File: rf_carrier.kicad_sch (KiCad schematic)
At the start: 1 part

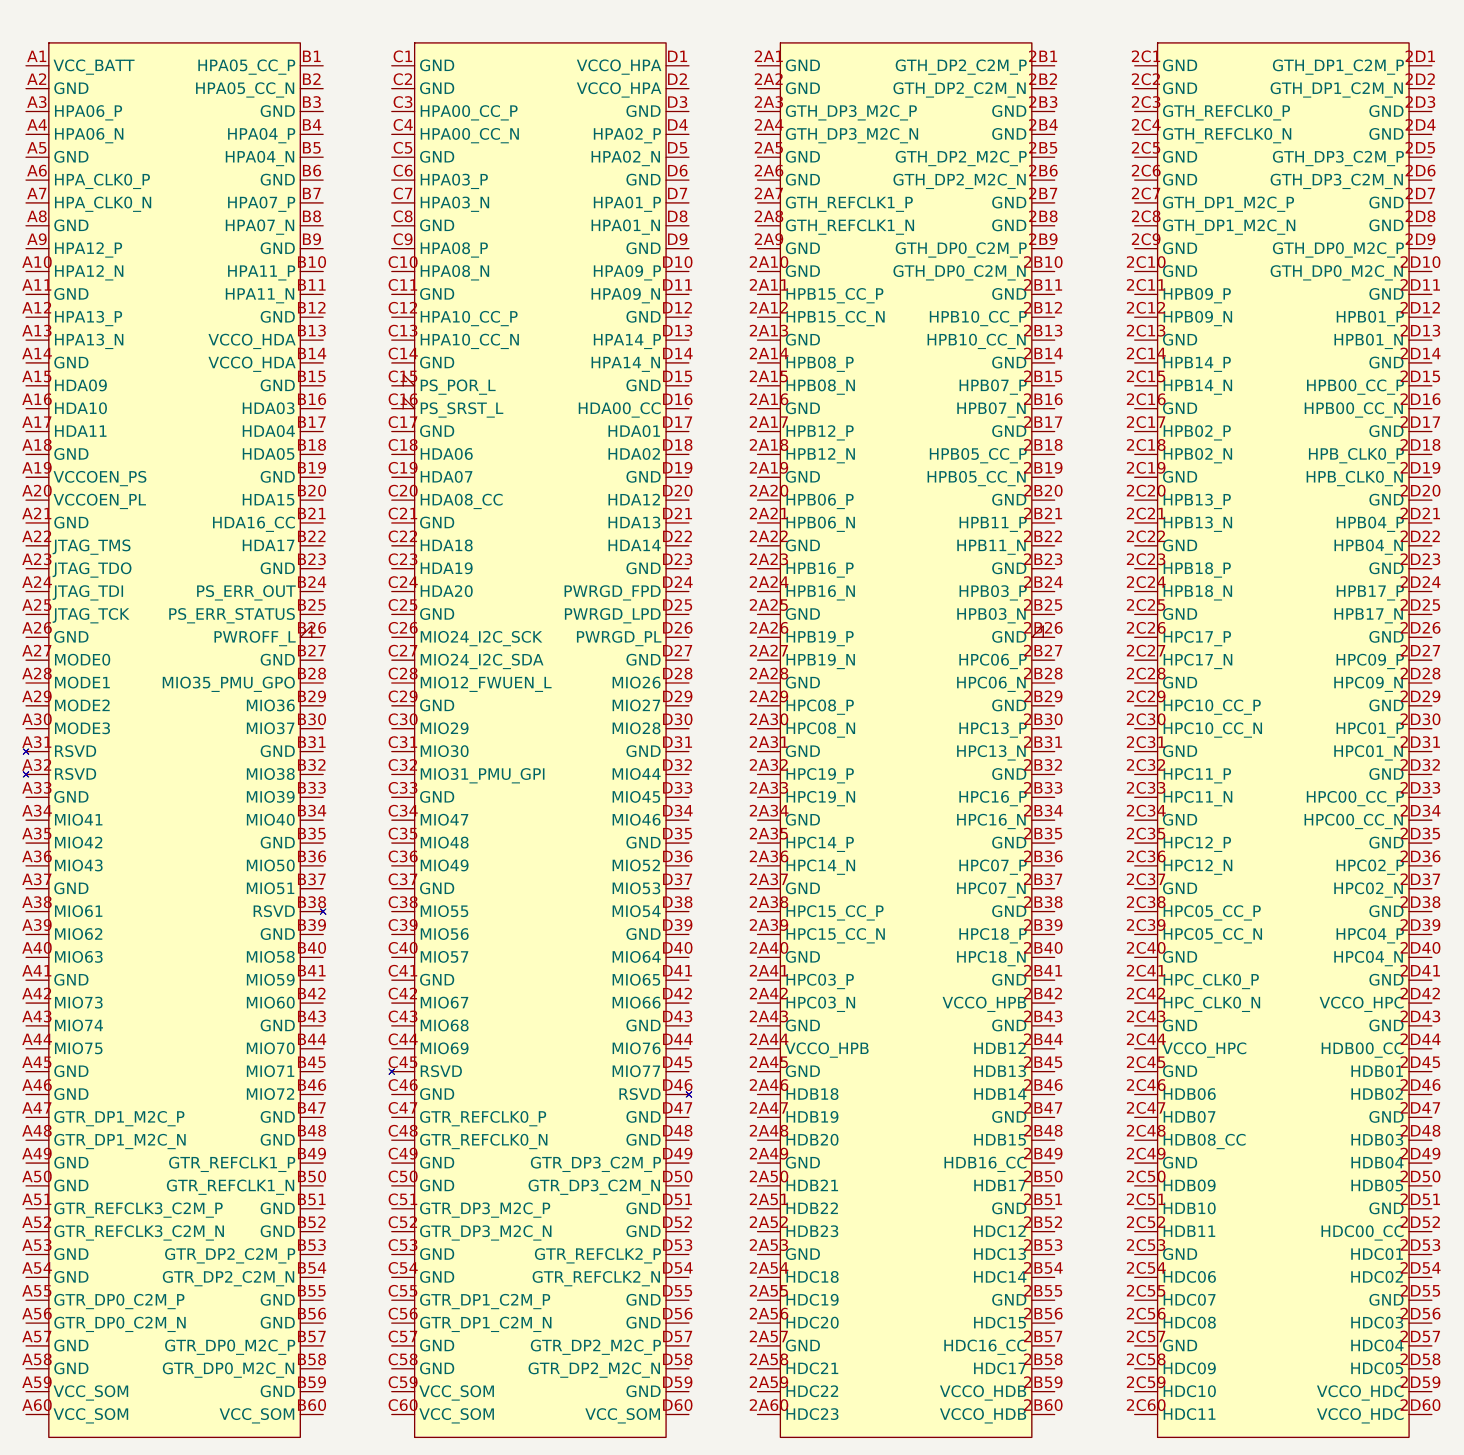
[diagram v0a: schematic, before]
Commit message: MIO pins hier labels and MIO25 symbol pin label fix
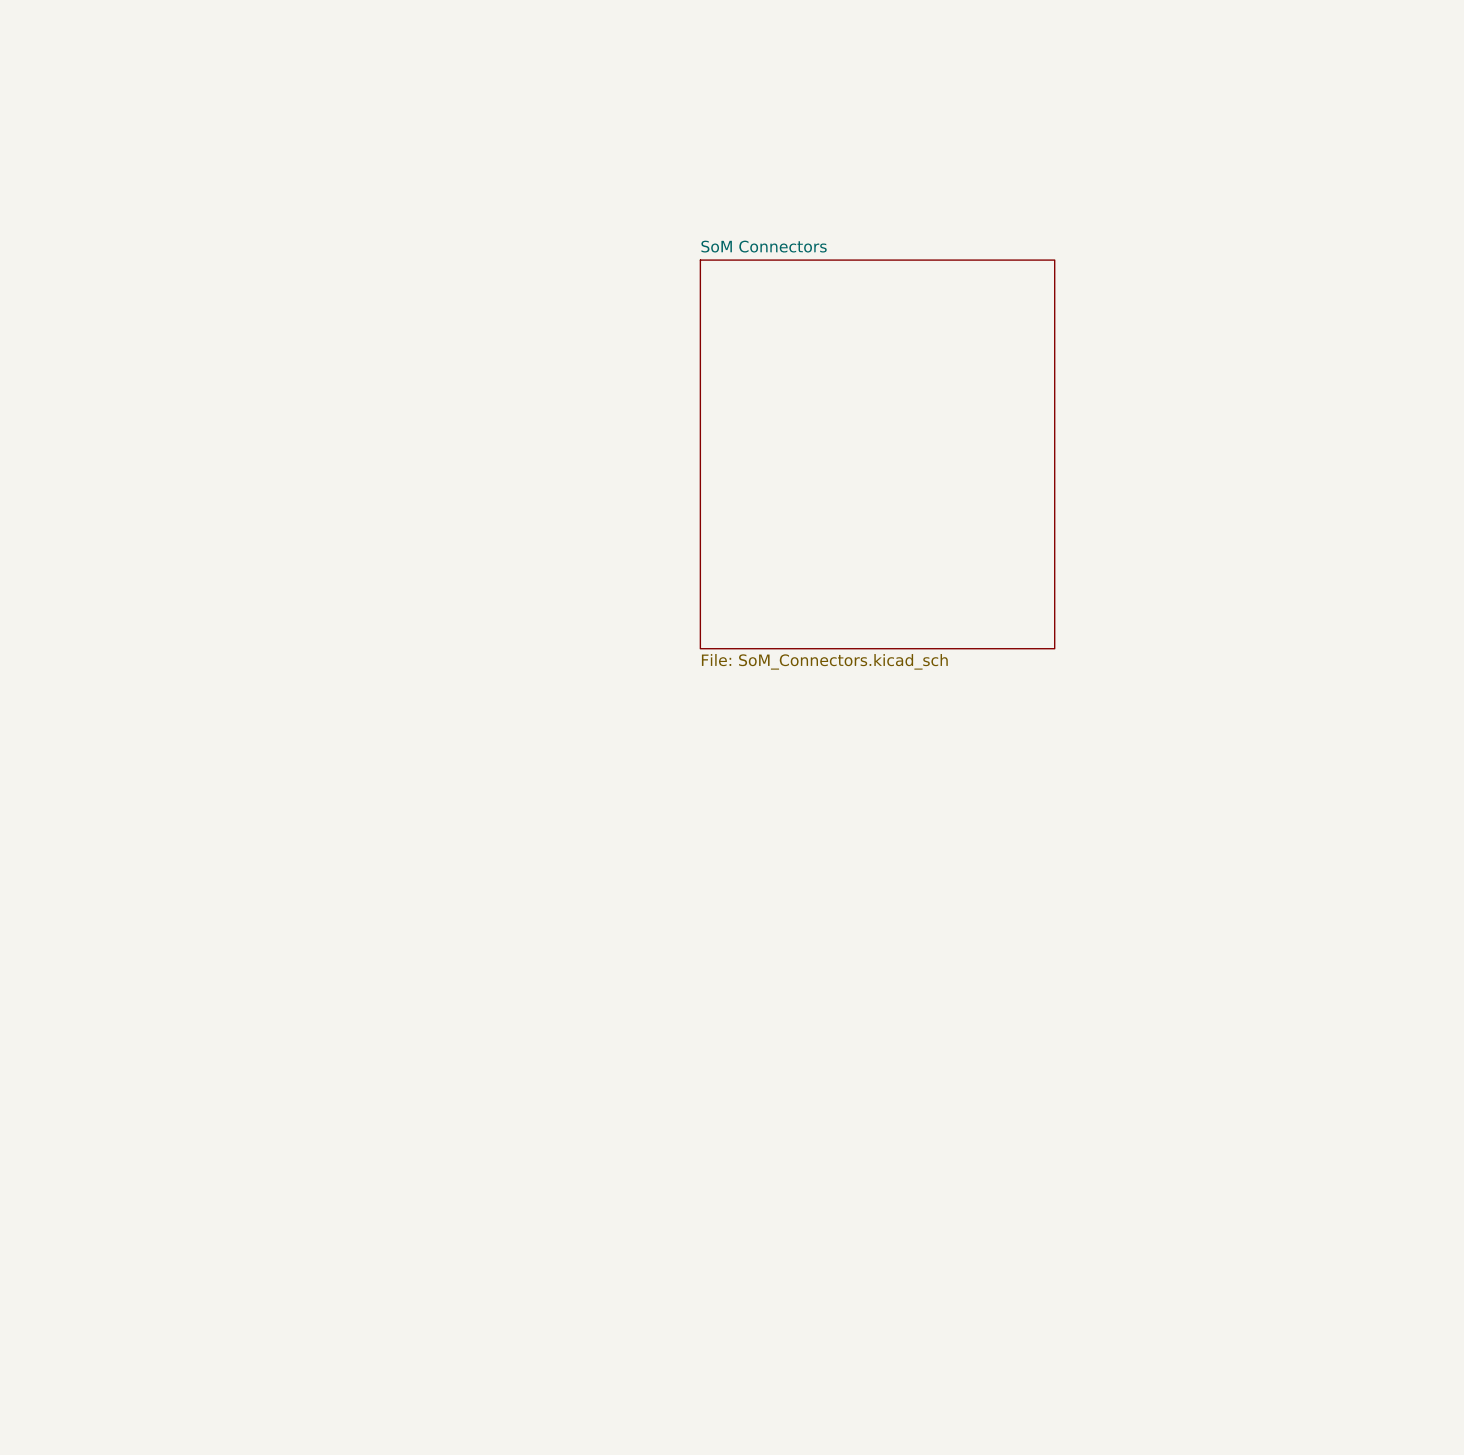
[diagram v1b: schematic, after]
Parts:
- removed U1: ~, parts:K26_SoM, symbol parts:K26_SoM
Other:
- added sheet SoM Connectors (SoM_Connectors.kicad_sch)

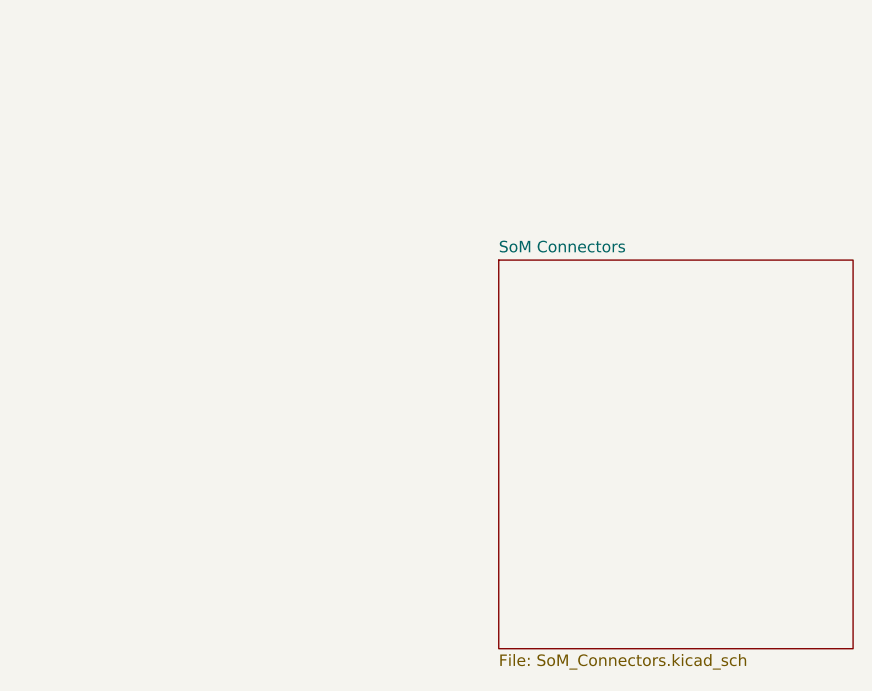
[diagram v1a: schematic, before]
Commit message: converted JTAG, GEM1, PCIE, and USB to busses
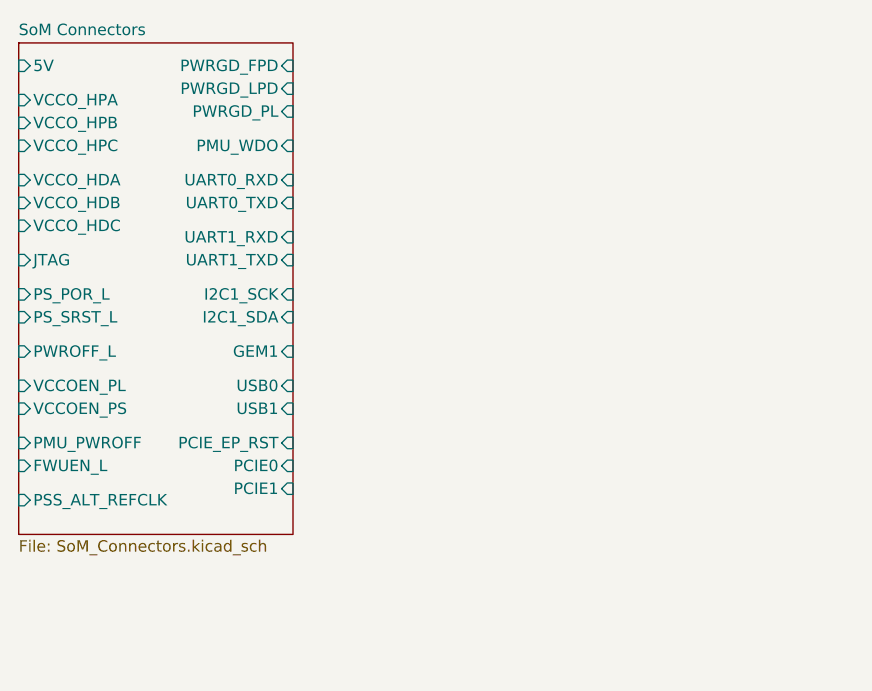
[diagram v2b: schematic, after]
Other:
- sheet SoM Connectors ports: added 5V, FWUEN_L, GEM1, I2C1_SCK, I2C1_SDA, JTAG, PCIE0, PCIE1, PCIE_EP_RST, PMU_PWROFF, PMU_WDO, PSS_ALT_REFCLK, PS_POR_L, PS_SRST_L, PWRGD_FPD, PWRGD_LPD, PWRGD_PL, PWROFF_L, UART0_RXD, UART0_TXD, UART1_RXD, UART1_TXD, USB0, USB1, VCCOEN_PL, VCCOEN_PS, VCCO_HDA, VCCO_HDB, VCCO_HDC, VCCO_HPA, VCCO_HPB, VCCO_HPC; removed none

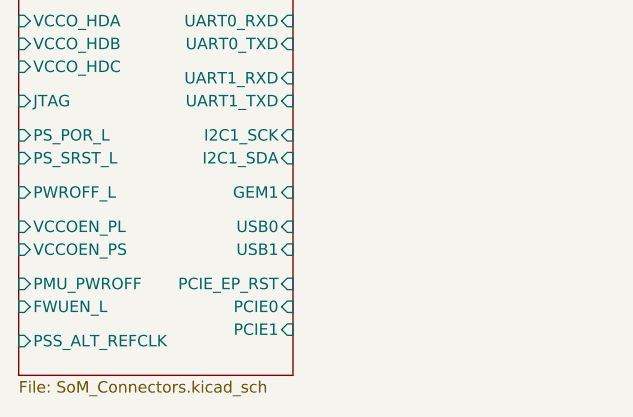
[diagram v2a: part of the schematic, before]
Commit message: preliminary USB-PD subcircuit bus labeling fixes
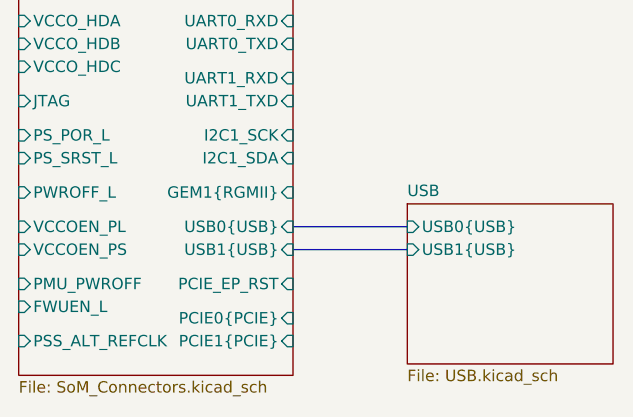
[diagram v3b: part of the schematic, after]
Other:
- added sheet USB (USB.kicad_sch)
- sheet SoM Connectors ports: added GEM1{RGMII}, PCIE0{PCIE}, PCIE1{PCIE}, USB0{USB}, USB1{USB}; removed GEM1, PCIE0, PCIE1, USB0, USB1
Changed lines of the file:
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@@
 	(generator_version "9.0")
 	(paper "A4")
+	(bus
+		(pts
+			(xy 78.74 66.04) (xy 91.44 66.04)
+		)
+		(stroke
+			(width 0)
+			(type default)
+		)
+	)
+	(bus
+		(pts
+			(xy 78.74 63.5) (xy 91.44 63.5)
+		)
+		(stroke
+			(width 0)
+			(type default)
+		)
+	)
 	(sheet
 		(at 48.26 25.4)
@@
 			)
 		)
-		(pin "GEM1" input
-			(at 78.74 59.69 0)
-			(effects
-				(font
-					(size 1.27 1.27)
-				)
-				(justify right)
-			)
-		)
 		(pin "JTAG" input
 			(at 48.26 49.53 180)
@@
 			)
 		)
-		(pin "PCIE0" input
-			(at 78.74 72.39 0)
-			(effects
-				(font
-					(size 1.27 1.27)
-				)
-				(justify right)
-			)
-		)
-		(pin "PCIE1" input
-			(at 78.74 74.93 0)
-			(effects
-				(font
-					(size 1.27 1.27)
-				)
-				(justify right)
-			)
-		)
-		(pin "USB0" input
+		(pin "GEM1{RGMII}" input
+			(at 78.74 59.69 0)
+			(effects
+				(font
+					(size 1.27 1.27)
+				)
+				(justify right)
+			)
+		)
+		(pin "PCIE0{PCIE}" input
+			(at 78.74 73.66 0)
+			(effects
+				(font
+					(size 1.27 1.27)
+				)
+				(justify right)
+			)
+		)
+		(pin "PCIE1{PCIE}" input
+			(at 78.74 76.2 0)
+			(effects
+				(font
+					(size 1.27 1.27)
+				)
+				(justify right)
+			)
+		)
+		(pin "USB0{USB}" input
 			(at 78.74 63.5 0)
 			(effects
@@
 			)
 		)
-		(pin "USB1" input
+		(pin "USB1{USB}" input
 			(at 78.74 66.04 0)
 			(effects
@@
 				)
 			)
+		)
+	)
+	(sheet
+		(at 91.44 60.96)
+		(size 22.86 17.78)
+		(exclude_from_sim no)
+		(in_bom yes)
+		(on_board yes)
+		(dnp no)
+		(fields_autoplaced yes)
+		(stroke
+			(width 0.1524)
+			(type solid)
+		)
+		(fill
+			(color 0 0 0 0.0000)
+		)
+		(property "Sheetname" "USB"
+			(at 91.44 60.2484 0)
+			(effects
+				(font
+					(size 1.27 1.27)
+				)
+				(justify left bottom)
+			)
+		)
+		(property "Sheetfile" "USB.kicad_sch"
+			(at 91.44 79.3246 0)
+			(effects
+				(font
+					(size 1.27 1.27)
+				)
+				(justify left top)
+			)
+		)
+		(pin "USB0{USB}" input
+			(at 91.44 63.5 180)
+			(effects
+				(font
+					(size 1.27 1.27)
+				)
+				(justify left)
+			)
+		)
+		(pin "USB1{USB}" input
+			(at 91.44 66.04 180)
+			(effects
+				(font
+					(size 1.27 1.27)
+				)
+				(justify left)
+			)
+		)
+		(instances
+			(project "rf_carrier"
+				(path "/1d5a0702-b67e-4abd-9b88-5b7f3ea07af2"
+					(page "3")
+				)
+			)

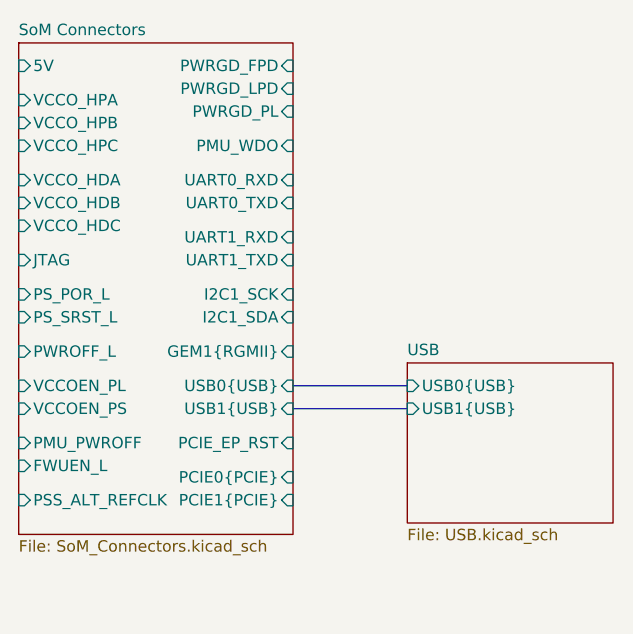
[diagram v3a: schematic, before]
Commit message: fixed USB0.SSTX connections fixed JTAG bus label adjust hier pins in top schematic fixed USB4750 footprint shield pins names
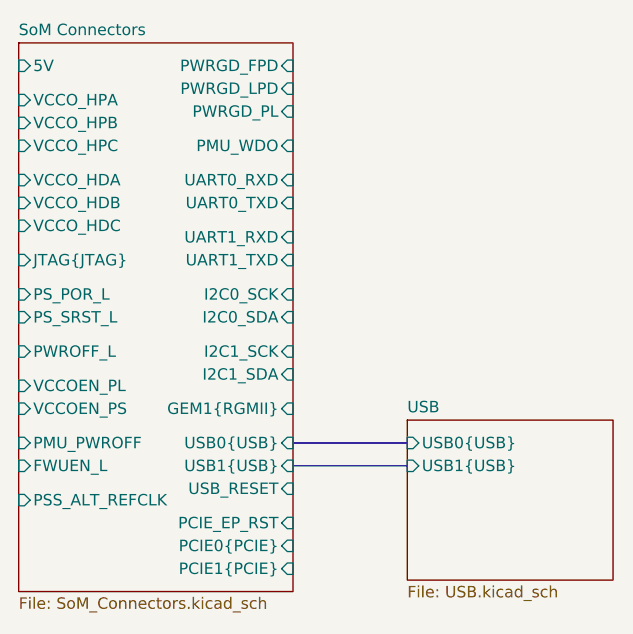
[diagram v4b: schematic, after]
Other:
- sheet SoM Connectors ports: added I2C0_SCK, I2C0_SDA, JTAG{JTAG}, USB_RESET; removed JTAG
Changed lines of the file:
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@@
 	(bus
 		(pts
-			(xy 78.74 66.04) (xy 91.44 66.04)
+			(xy 78.74 72.39) (xy 91.44 72.39)
 		)
 		(stroke
@@
 	(bus
 		(pts
-			(xy 78.74 63.5) (xy 91.44 63.5)
+			(xy 78.74 69.85) (xy 91.44 69.85)
 		)
 		(stroke
@@
 	(sheet
 		(at 48.26 25.4)
-		(size 30.48 54.61)
+		(size 30.48 60.96)
 		(exclude_from_sim no)
 		(in_bom yes)
@@
 		)
 		(property "Sheetfile" "SoM_Connectors.kicad_sch"
-			(at 48.26 80.5946 0)
+			(at 48.26 86.9446 0)
 			(effects
 				(font
@@
 		)
 		(pin "I2C1_SCK" input
-			(at 78.74 53.34 0)
+			(at 78.74 59.69 0)
 			(effects
 				(font
@@
 		)
 		(pin "I2C1_SDA" input
-			(at 78.74 55.88 0)
+			(at 78.74 62.23 0)
 			(effects
 				(font
@@
 		)
 		(pin "PCIE_EP_RST" input
-			(at 78.74 69.85 0)
+			(at 78.74 78.74 0)
 			(effects
 				(font
@@
 			)
 		)
-		(pin "JTAG" input
+		(pin "I2C0_SCK" input
+			(at 78.74 53.34 0)
+			(effects
+				(font
+					(size 1.27 1.27)
+				)
+				(justify right)
+			)
+		)
+		(pin "I2C0_SDA" input
+			(at 78.74 55.88 0)
+			(effects
+				(font
+					(size 1.27 1.27)
+				)
+				(justify right)
+			)
+		)
+		(pin "JTAG{JTAG}" input
 			(at 48.26 49.53 180)
 			(effects
@@
 			)
 		)
+		(pin "USB_RESET" input
+			(at 78.74 74.93 0)
+			(effects
+				(font
+					(size 1.27 1.27)
+				)
+				(justify right)
+			)
+		)
 		(pin "GEM1{RGMII}" input
-			(at 78.74 59.69 0)
+			(at 78.74 66.04 0)
 			(effects
 				(font
@@
 		)
 		(pin "PCIE0{PCIE}" input
-			(at 78.74 73.66 0)
+			(at 78.74 81.28 0)
 			(effects
 				(font
@@
 		)
 		(pin "PCIE1{PCIE}" input
-			(at 78.74 76.2 0)
+			(at 78.74 83.82 0)
 			(effects
 				(font
@@
 		)
 		(pin "USB0{USB}" input
-			(at 78.74 63.5 0)
+			(at 78.74 69.85 0)
 			(effects
 				(font
@@
 		)
 		(pin "USB1{USB}" input
-			(at 78.74 66.04 0)
+			(at 78.74 72.39 0)
 			(effects
 				(font
@@
 	)
 	(sheet
-		(at 91.44 60.96)
+		(at 91.44 67.31)
 		(size 22.86 17.78)
 		(exclude_from_sim no)
@@
 		)
 		(property "Sheetname" "USB"
-			(at 91.44 60.2484 0)
+			(at 91.44 66.5984 0)
 			(effects
 				(font
@@
 		)
 		(property "Sheetfile" "USB.kicad_sch"
-			(at 91.44 79.3246 0)
+			(at 91.44 85.6746 0)
 			(effects
 				(font
@@
 		)
 		(pin "USB0{USB}" input
-			(at 91.44 63.5 180)
+			(at 91.44 69.85 180)
 			(effects
 				(font
@@
 		)
 		(pin "USB1{USB}" input
-			(at 91.44 66.04 180)
-			(effects
-				(font
+			(at 91.44 72.39 180)
+			(effects
+				(font

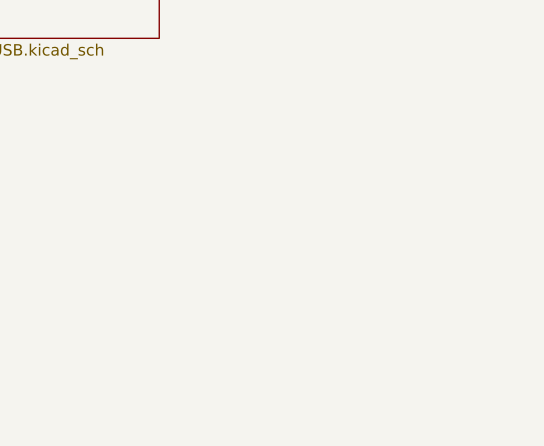
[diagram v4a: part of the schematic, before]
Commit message: add battery charger
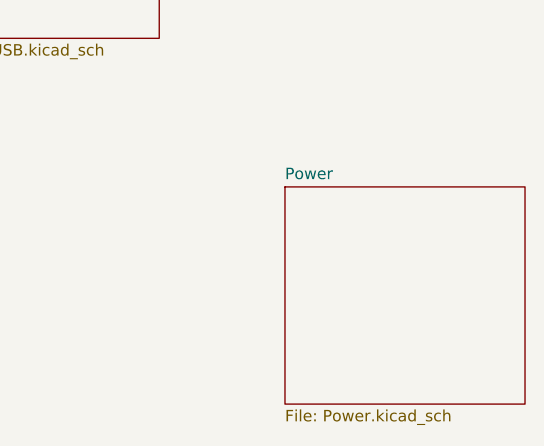
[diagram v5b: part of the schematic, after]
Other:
- added sheet Power (Power.kicad_sch)
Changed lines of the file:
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@@
+	)
+	(sheet
+		(at 128.27 101.6)
+		(size 26.67 24.13)
+		(exclude_from_sim no)
+		(in_bom yes)
+		(on_board yes)
+		(dnp no)
+		(fields_autoplaced yes)
+		(stroke
+			(width 0.1524)
+			(type solid)
+		)
+		(fill
+			(color 0 0 0 0.0000)
+		)
+		(property "Sheetname" "Power"
+			(at 128.27 100.8884 0)
+			(effects
+				(font
+					(size 1.27 1.27)
+				)
+				(justify left bottom)
+			)
+		)
+		(property "Sheetfile" "Power.kicad_sch"
+			(at 128.27 126.3146 0)
+			(effects
+				(font
+					(size 1.27 1.27)
+				)
+				(justify left top)
+			)
+		)
+		(instances
+			(project "rf_carrier"
+				(path "/1d5a0702-b67e-4abd-9b88-5b7f3ea07af2"
+					(page "6")
+				)
+			)
+		)
 	)
 	(sheet
